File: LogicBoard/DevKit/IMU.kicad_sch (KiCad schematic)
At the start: 5 parts, among them U3 LSM6DS3TR-C

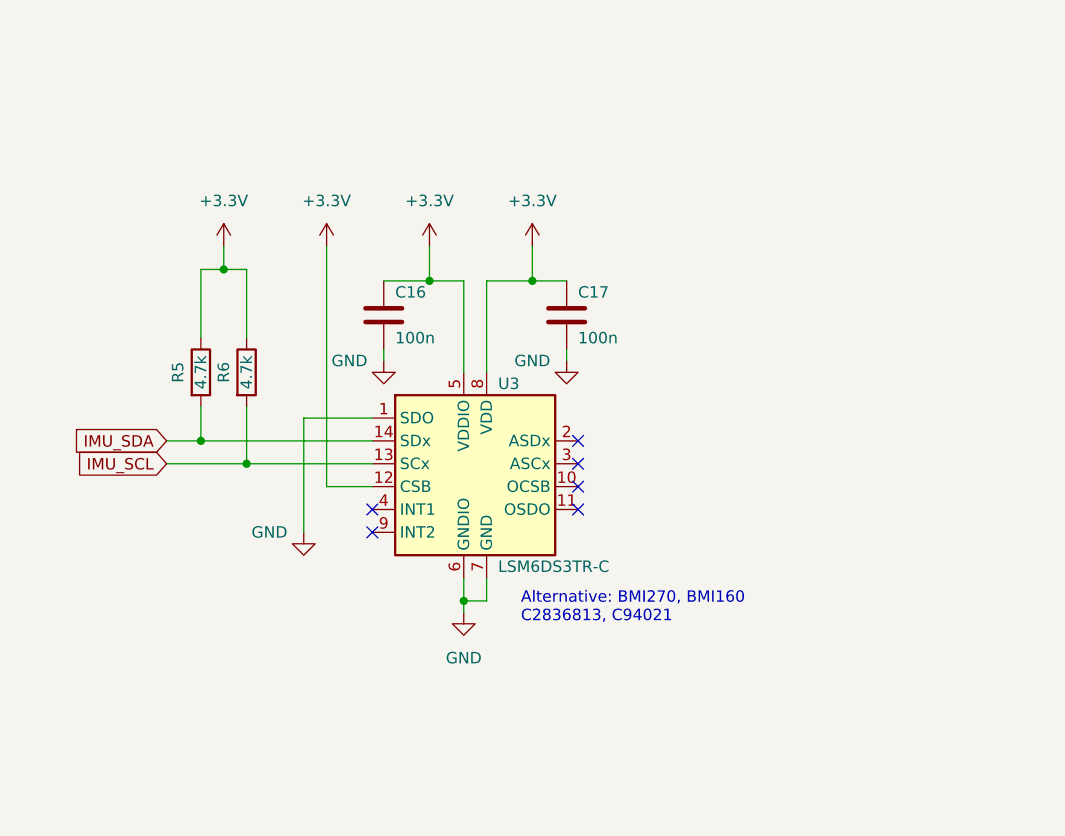
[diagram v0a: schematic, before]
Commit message: v3.3.2 - ECP2304 changes
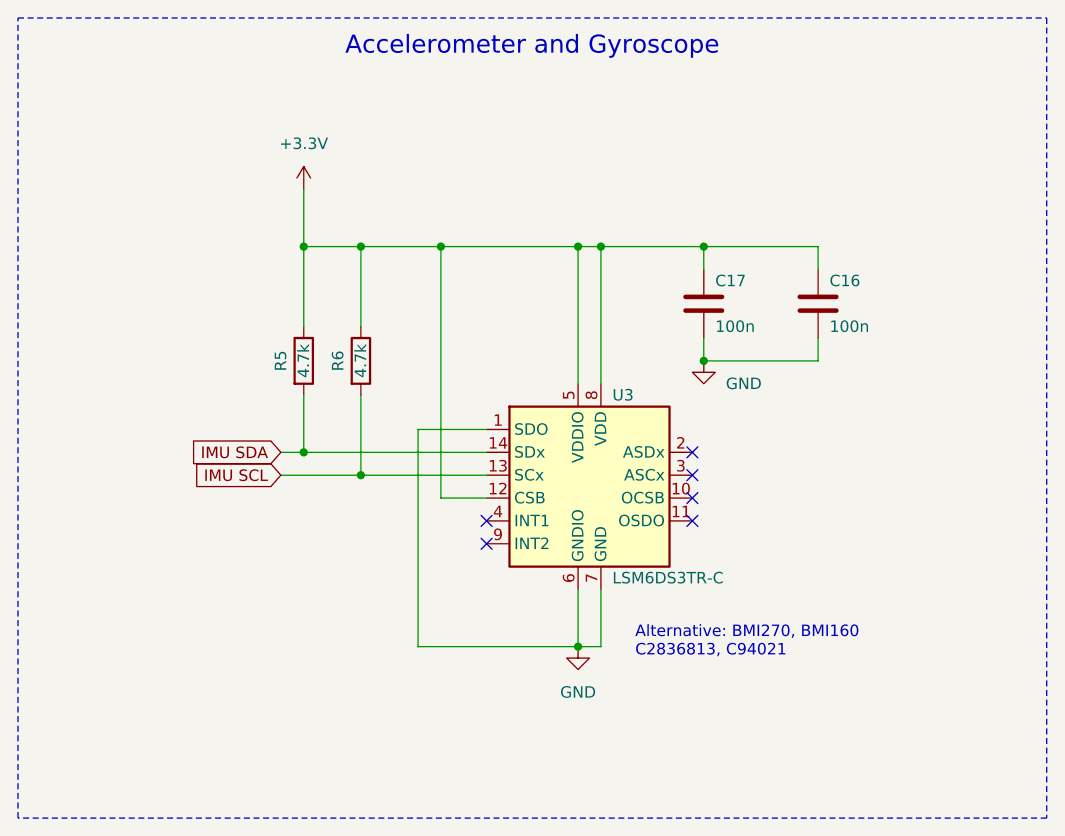
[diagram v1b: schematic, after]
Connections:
- net IMU_SCL renamed IMU SCL
- net IMU_SDA renamed IMU SDA
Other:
- note added: "Accelerometer and Gyroscope"
- moved on the sheet: C16, C17, R5, R6, U3
